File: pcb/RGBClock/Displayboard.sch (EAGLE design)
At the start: 66 parts, among them U1 LP3878MR-ADJ, U10 MCP23017SO, U2 P82B96DR, U3 P82B96DR, U4 PCA9685PW, U5 TPS71533DCKR, U6 ZXLD1362ET5TA, U7 74HCT1G14GW, U8 74HCT1G86GW, U9 TPA0172-HTSSOP24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

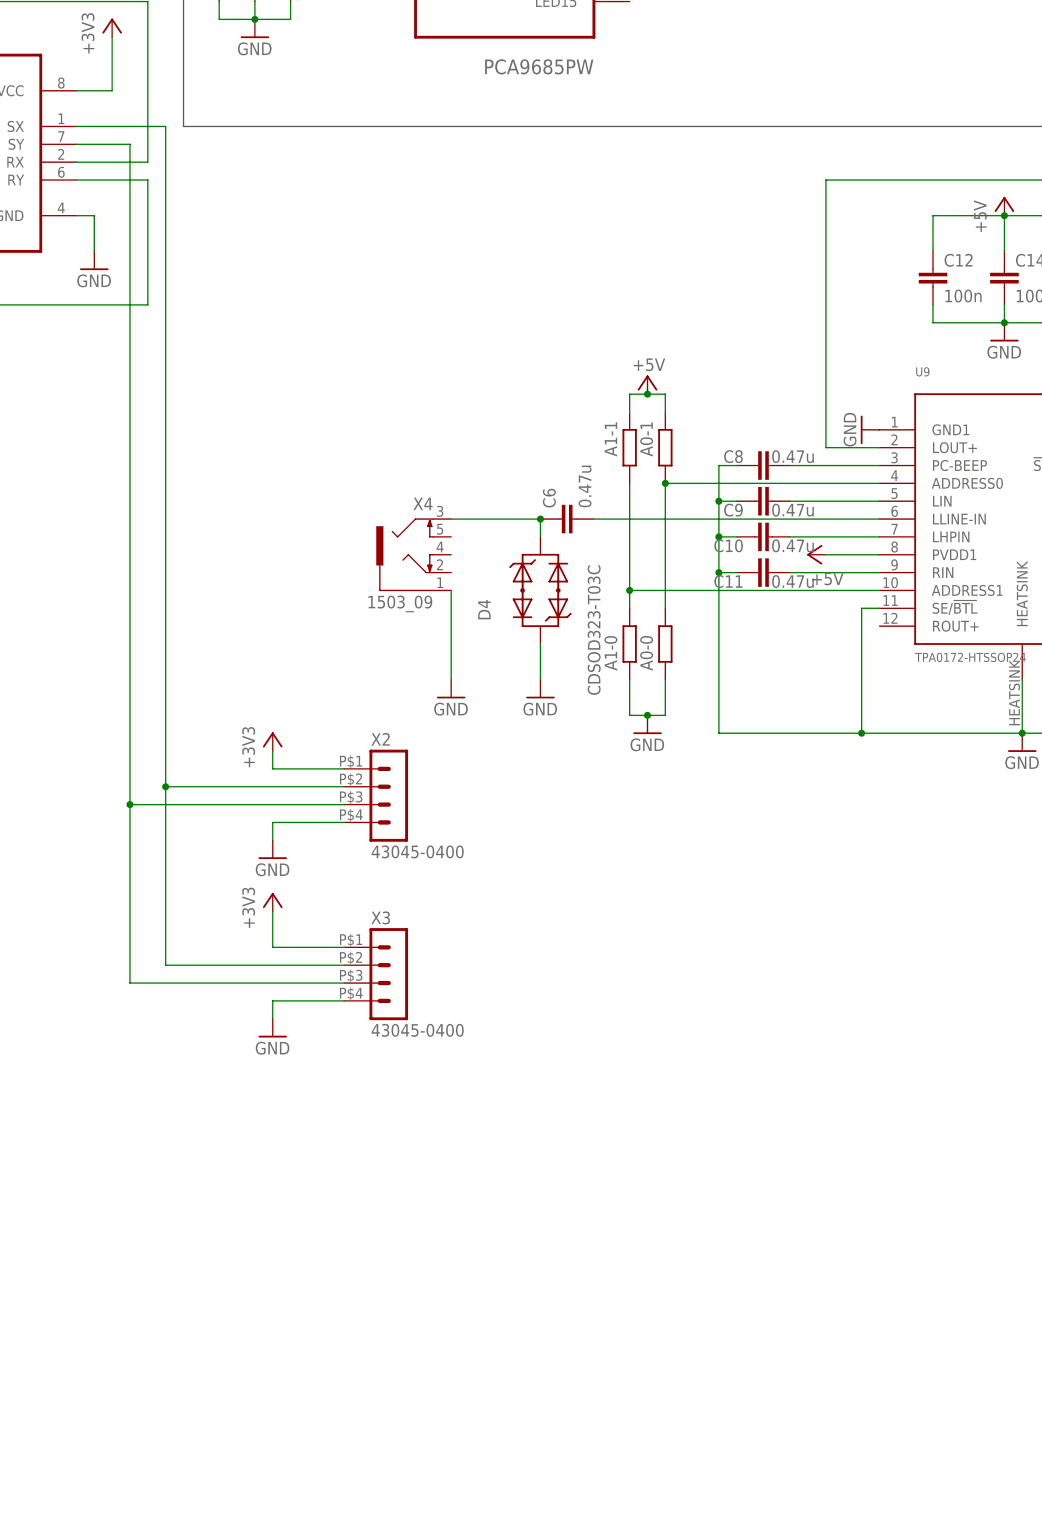
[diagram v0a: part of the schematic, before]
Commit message: Adding analog power and light sensor
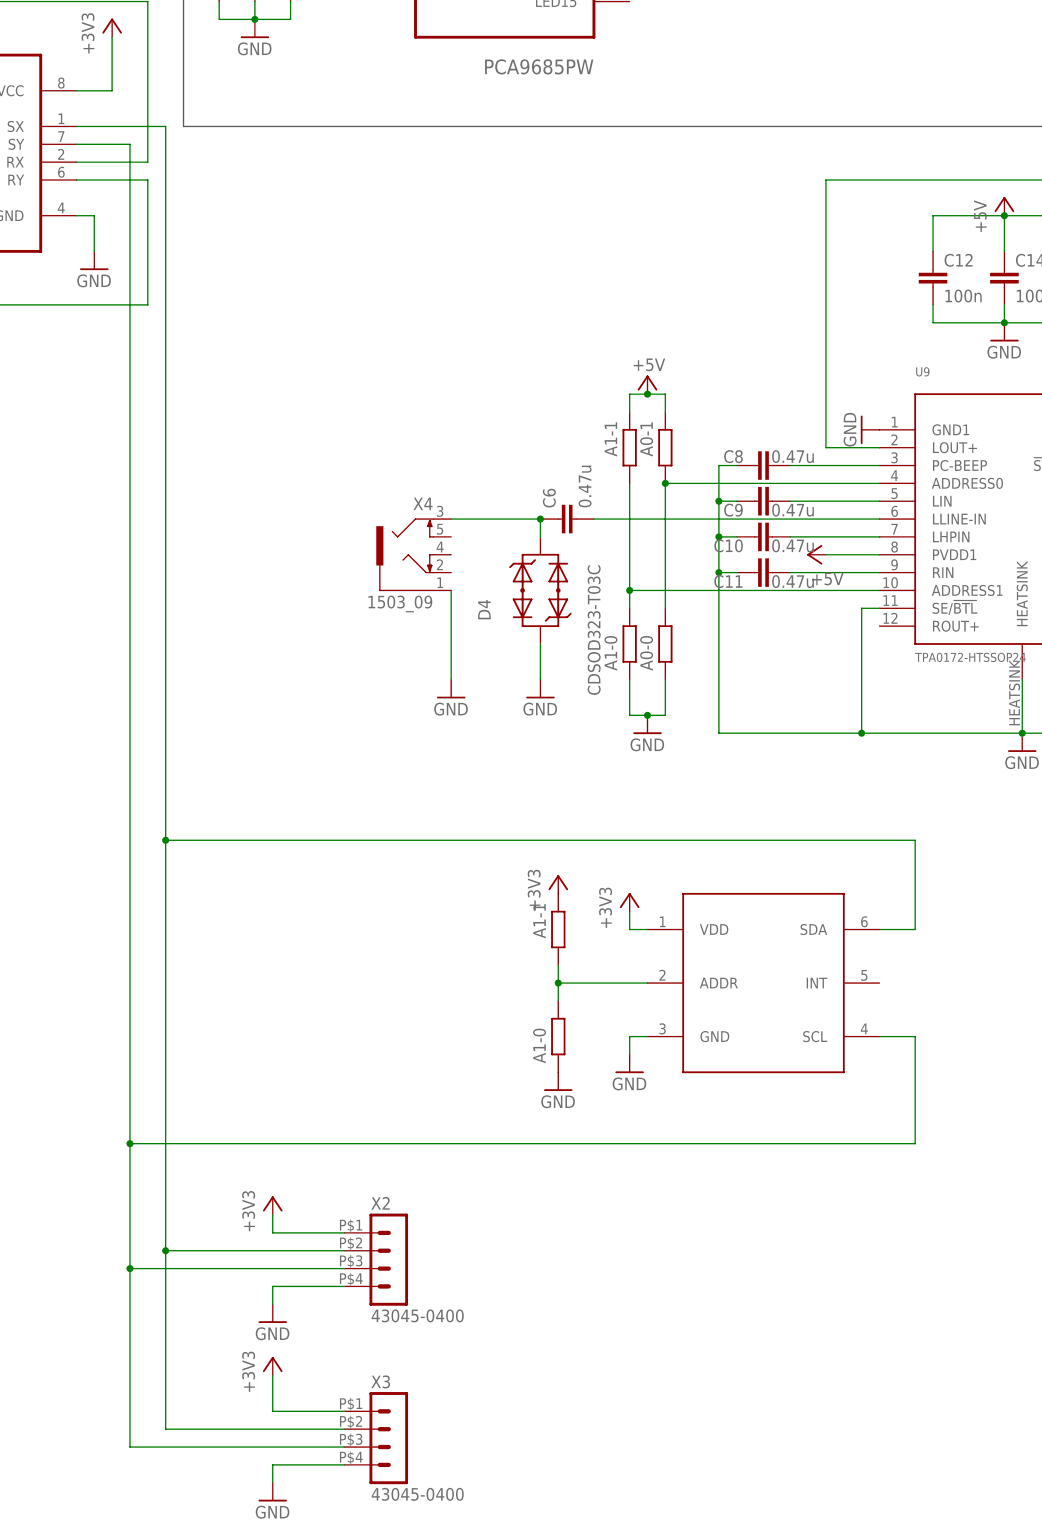
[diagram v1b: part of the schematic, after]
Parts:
- added R27: A1-1, resistor:R-EU_R0402
- added R28: A1-0, resistor:R-EU_R0402
- added U11: TSL2561, MyComponents:TSL2561
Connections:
- new net N$34: R27.1, R28.2, U11.ADDR
- net +3V3: now also R27.2, U11.VDD
- net GND: now also R28.1, U11.GND
- net N$7: now also U11.SDA
- net N$9: now also U11.SCL
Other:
- moved on the sheet: X2, X3
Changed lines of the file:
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@@
 <part name="C19" library="rcl" deviceset="C-EU" device="C0805" value="22n"/>
 <part name="GND27" library="supply1" deviceset="GND" device=""/>
+<part name="U11" library="MyComponents" deviceset="TSL2561" device=""/>
+<part name="GND28" library="supply1" deviceset="GND" device=""/>
+<part name="+3V5" library="supply1" deviceset="+3V3" device=""/>
+<part name="R27" library="resistor" deviceset="R-EU_" device="R0402" value="A1-1"/>
+<part name="R28" library="resistor" deviceset="R-EU_" device="R0402" value="A1-0"/>
+<part name="GND29" library="supply1" deviceset="GND" device=""/>
+<part name="+3V6" library="supply1" deviceset="+3V3" device=""/>
 </parts>
 <sheets>
@@
 <instance part="P+4" gate="1" x="383.54" y="-7.62" rot="R90"/>
 <instance part="GND5" gate="1" x="401.32" y="-12.7"/>
-<instance part="X2" gate="G$1" x="119.38" y="-96.52"/>
-<instance part="X3" gate="G$1" x="119.38" y="-121.92"/>
+<instance part="X2" gate="G$1" x="119.38" y="-162.56"/>
+<instance part="X3" gate="G$1" x="119.38" y="-187.96"/>
 <instance part="X5" gate="G$1" x="241.3" y="-10.16"/>
 <instance part="X6" gate="G$1" x="294.64" y="78.74"/>
-<instance part="+3V3" gate="G$1" x="104.14" y="-86.36"/>
-<instance part="+3V4" gate="G$1" x="104.14" y="-109.22"/>
-<instance part="GND7" gate="1" x="104.14" y="-104.14"/>
-<instance part="GND8" gate="1" x="104.14" y="-129.54"/>
+<instance part="+3V3" gate="G$1" x="104.14" y="-152.4"/>
+<instance part="+3V4" gate="G$1" x="104.14" y="-175.26"/>
+<instance part="GND7" gate="1" x="104.14" y="-170.18"/>
+<instance part="GND8" gate="1" x="104.14" y="-195.58"/>
 <instance part="GND9" gate="1" x="210.82" y="-88.9"/>
 <instance part="P+5" gate="1" x="248.92" y="-30.48"/>
@@
 </instance>
 <instance part="GND27" gate="1" x="342.9" y="-101.6"/>
+<instance part="U11" gate="G$1" x="172.72" y="-121.92"/>
+<instance part="GND28" gate="1" x="154.94" y="-134.62"/>
+<instance part="+3V5" gate="G$1" x="154.94" y="-109.22"/>
+<instance part="R27" gate="G$1" x="144.78" y="-114.3" smashed="yes" rot="R90">
+<attribute name="VALUE" x="143.002" y="-115.57" size="1.778" layer="96" rot="R90"/>
+</instance>
+<instance part="R28" gate="G$1" x="144.78" y="-129.54" smashed="yes" rot="R90">
+<attribute name="VALUE" x="143.002" y="-133.35" size="1.778" layer="96" rot="R90"/>
+</instance>
+<instance part="GND29" gate="1" x="144.78" y="-137.16"/>
+<instance part="+3V6" gate="G$1" x="144.78" y="-106.68"/>
 </instances>
 <busses>
@@
 <segment>
 <pinref part="GND7" gate="1" pin="GND"/>
-<wire x1="104.14" y1="-101.6" x2="104.14" y2="-99.06" width="0.1524" layer="91"/>
+<wire x1="104.14" y1="-167.64" x2="104.14" y2="-165.1" width="0.1524" layer="91"/>
 <pinref part="X2" gate="G$1" pin="4"/>
-<wire x1="104.14" y1="-99.06" x2="114.3" y2="-99.06" width="0.1524" layer="91"/>
+<wire x1="104.14" y1="-165.1" x2="114.3" y2="-165.1" width="0.1524" layer="91"/>
 </segment>
 <segment>
 <pinref part="GND8" gate="1" pin="GND"/>
-<wire x1="104.14" y1="-127" x2="104.14" y2="-124.46" width="0.1524" layer="91"/>
+<wire x1="104.14" y1="-193.04" x2="104.14" y2="-190.5" width="0.1524" layer="91"/>
 <pinref part="X3" gate="G$1" pin="4"/>
-<wire x1="104.14" y1="-124.46" x2="114.3" y2="-124.46" width="0.1524" layer="91"/>
+<wire x1="104.14" y1="-190.5" x2="114.3" y2="-190.5" width="0.1524" layer="91"/>
 </segment>
 <segment>
@@
 <pinref part="GND27" gate="1" pin="GND"/>
 </segment>
+<segment>
+<pinref part="R28" gate="G$1" pin="1"/>
+<pinref part="GND29" gate="1" pin="GND"/>
+</segment>
+<segment>
+<pinref part="U11" gate="G$1" pin="GND"/>
+<pinref part="GND28" gate="1" pin="GND"/>
+<wire x1="157.48" y1="-129.54" x2="154.94" y2="-129.54" width="0.1524" layer="91"/>
+<wire x1="154.94" y1="-129.54" x2="154.94" y2="-132.08" width="0.1524" layer="91"/>
+</segment>
 </net>
 <net name="VCC" class="2">
@@
 <segment>
 <pinref part="+3V3" gate="G$1" pin="+3V3"/>
-<wire x1="104.14" y1="-88.9" x2="104.14" y2="-91.44" width="0.1524" layer="91"/>
+<wire x1="104.14" y1="-154.94" x2="104.14" y2="-157.48" width="0.1524" layer="91"/>
 <pinref part="X2" gate="G$1" pin="1"/>
-<wire x1="104.14" y1="-91.44" x2="114.3" y2="-91.44" width="0.1524" layer="91"/>
+<wire x1="104.14" y1="-157.48" x2="114.3" y2="-157.48" width="0.1524" layer="91"/>
 </segment>
 <segment>
 <pinref part="+3V4" gate="G$1" pin="+3V3"/>
-<wire x1="104.14" y1="-111.76" x2="104.14" y2="-116.84" width="0.1524" layer="91"/>
+<wire x1="104.14" y1="-177.8" x2="104.14" y2="-182.88" width="0.1524" layer="91"/>
 <pinref part="X3" gate="G$1" pin="1"/>
-<wire x1="104.14" y1="-116.84" x2="114.3" y2="-116.84" width="0.1524" layer="91"/>
+<wire x1="104.14" y1="-182.88" x2="114.3" y2="-182.88" width="0.1524" layer="91"/>
+</segment>
+<segment>
+<pinref part="R27" gate="G$1" pin="2"/>
+<pinref part="+3V6" gate="G$1" pin="+3V3"/>
+</segment>
+<segment>
+<pinref part="+3V5" gate="G$1" pin="+3V3"/>
+<wire x1="154.94" y1="-111.76" x2="154.94" y2="-114.3" width="0.1524" layer="91"/>
+<pinref part="U11" gate="G$1" pin="VDD"/>
+<wire x1="154.94" y1="-114.3" x2="157.48" y2="-114.3" width="0.1524" layer="91"/>
 </segment>
 </net>
@@
 <pinref part="U3" gate="A" pin="SY"/>
 <wire x1="76.2" y1="-2.54" x2="83.82" y2="-2.54" width="0.1524" layer="91"/>
-<wire x1="83.82" y1="-2.54" x2="83.82" y2="-96.52" width="0.1524" layer="91"/>
+<wire x1="83.82" y1="-2.54" x2="83.82" y2="-144.78" width="0.1524" layer="91"/>
 <pinref part="X3" gate="G$1" pin="3"/>
-<wire x1="83.82" y1="-96.52" x2="83.82" y2="-121.92" width="0.1524" layer="91"/>
-<wire x1="83.82" y1="-121.92" x2="114.3" y2="-121.92" width="0.1524" layer="91"/>
+<wire x1="83.82" y1="-144.78" x2="83.82" y2="-162.56" width="0.1524" layer="91"/>
+<wire x1="83.82" y1="-162.56" x2="83.82" y2="-187.96" width="0.1524" layer="91"/>
+<wire x1="83.82" y1="-187.96" x2="114.3" y2="-187.96" width="0.1524" layer="91"/>
 <pinref part="X2" gate="G$1" pin="3"/>
-<wire x1="83.82" y1="-96.52" x2="114.3" y2="-96.52" width="0.1524" layer="91"/>
-<junction x="83.82" y="-96.52"/>
+<wire x1="83.82" y1="-162.56" x2="114.3" y2="-162.56" width="0.1524" layer="91"/>
+<junction x="83.82" y="-162.56"/>
+<pinref part="U11" gate="G$1" pin="SCL"/>
+<wire x1="190.5" y1="-129.54" x2="195.58" y2="-129.54" width="0.1524" layer="91"/>
+<wire x1="195.58" y1="-129.54" x2="195.58" y2="-144.78" width="0.1524" layer="91"/>
+<wire x1="195.58" y1="-144.78" x2="83.82" y2="-144.78" width="0.1524" layer="91"/>
+<junction x="83.82" y="-144.78"/>
 </segment>
 </net>
@@
 <pinref part="U3" gate="A" pin="SX"/>
 <wire x1="76.2" y1="0" x2="88.9" y2="0" width="0.1524" layer="91"/>
-<wire x1="88.9" y1="0" x2="88.9" y2="-93.98" width="0.1524" layer="91"/>
-<wire x1="88.9" y1="-93.98" x2="88.9" y2="-119.38" width="0.1524" layer="91"/>
+<wire x1="88.9" y1="0" x2="88.9" y2="-101.6" width="0.1524" layer="91"/>
+<wire x1="88.9" y1="-101.6" x2="88.9" y2="-160.02" width="0.1524" layer="91"/>
+<wire x1="88.9" y1="-160.02" x2="88.9" y2="-185.42" width="0.1524" layer="91"/>
 <pinref part="X2" gate="G$1" pin="2"/>
-<wire x1="88.9" y1="-93.98" x2="114.3" y2="-93.98" width="0.1524" layer="91"/>
-<junction x="88.9" y="-93.98"/>
+<wire x1="88.9" y1="-160.02" x2="114.3" y2="-160.02" width="0.1524" layer="91"/>
+<junction x="88.9" y="-160.02"/>
 <pinref part="X3" gate="G$1" pin="2"/>
-<wire x1="88.9" y1="-119.38" x2="114.3" y2="-119.38" width="0.1524" layer="91"/>
+<wire x1="88.9" y1="-185.42" x2="114.3" y2="-185.42" width="0.1524" layer="91"/>
+<wire x1="88.9" y1="-101.6" x2="195.58" y2="-101.6" width="0.1524" layer="91"/>
+<wire x1="195.58" y1="-101.6" x2="195.58" y2="-114.3" width="0.1524" layer="91"/>
+<pinref part="U11" gate="G$1" pin="SDA"/>
+<wire x1="195.58" y1="-114.3" x2="190.5" y2="-114.3" width="0.1524" layer="91"/>
+<junction x="88.9" y="-101.6"/>
 </segment>
 </net>
@@
 </segment>
 </net>
+<net name="N$34" class="0">
+<segment>
+<pinref part="R27" gate="G$1" pin="1"/>
+<pinref part="R28" gate="G$1" pin="2"/>
+<wire x1="144.78" y1="-119.38" x2="144.78" y2="-121.92" width="0.1524" layer="91"/>
+<wire x1="144.78" y1="-121.92" x2="144.78" y2="-124.46" width="0.1524" layer="91"/>
+<pinref part="U11" gate="G$1" pin="ADDR"/>
+<wire x1="144.78" y1="-121.92" x2="157.48" y2="-121.92" width="0.1524" layer="91"/>
+<junction x="144.78" y="-121.92"/>
+</segment>
+</net>

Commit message: Main and Display updated
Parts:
- C1, C7: device rcl:C-EUC1206 -> rcl:C-EUC0805
- C15, C4: device rcl:C-EUC2012 -> rcl:C-EUC0805
- C2, C3: device rcl:C-EUC1608 -> rcl:C-EUC0805
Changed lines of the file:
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@@
 <setting verticaltext="up"/>
 </settings>
-<grid distance="0.1" unitdist="inch" unit="inch" style="lines" multiple="1" display="no" altdistance="0.01" altunitdist="inch" altunit="inch"/>
+<grid distance="50" unitdist="mil" unit="mil" style="lines" multiple="1" display="no" altdistance="0.01" altunitdist="inch" altunit="inch"/>
 <layers>
 <layer number="1" name="Top" color="4" fill="1" visible="no" active="no"/>
@@
 <part name="P+8" library="supply1" deviceset="+5V" device=""/>
 <part name="C5" library="rcl" deviceset="C-EU" device="C0805" value="100n"/>
-<part name="C7" library="rcl" deviceset="C-EU" device="C1206" value="0,47u"/>
+<part name="C7" library="rcl" deviceset="C-EU" device="C0805" value="0,47u"/>
 <part name="C12" library="rcl" deviceset="C-EU" device="C0805" value="100n"/>
 <part name="C14" library="rcl" deviceset="C-EU" device="C0805" value="100n"/>
@@
 <part name="GND19" library="supply1" deviceset="GND" device=""/>
 <part name="C18" library="rcl" deviceset="C-EU" device="C0805" value="0.47u"/>
-<part name="C15" library="rcl" deviceset="C-EU" device="C2012" value="10u"/>
-<part name="C1" library="rcl" deviceset="C-EU" device="C1206" value="4u7"/>
-<part name="C2" library="rcl" deviceset="C-EU" device="C1608" value="10n"/>
-<part name="C3" library="rcl" deviceset="C-EU" device="C1608" value="680p"/>
+<part name="C15" library="rcl" deviceset="C-EU" device="C0805" value="10u"/>
+<part name="C1" library="rcl" deviceset="C-EU" device="C0805" value="4u7"/>
+<part name="C2" library="rcl" deviceset="C-EU" device="C0805" value="10n"/>
+<part name="C3" library="rcl" deviceset="C-EU" device="C0805" value="680p"/>
 <part name="R1" library="resistor" deviceset="R-EU_" device="R0603" value="4.02k"/>
 <part name="R2" library="resistor" deviceset="R-EU_" device="R0603" value="1k"/>
 <part name="GND20" library="supply1" deviceset="GND" device=""/>
-<part name="C4" library="rcl" deviceset="C-EU" device="C2012" value="10u"/>
+<part name="C4" library="rcl" deviceset="C-EU" device="C0805" value="10u"/>
 <part name="GND21" library="supply1" deviceset="GND" device=""/>
 <part name="GND22" library="supply1" deviceset="GND" device=""/>
@@
 <instance part="GND19" gate="1" x="172.72" y="114.3"/>
 <instance part="C18" gate="G$1" x="256.54" y="-76.2" smashed="yes" rot="R180">
-<attribute name="NAME" x="262.636" y="-76.581" size="1.778" layer="95" rot="R180"/>
-<attribute name="VALUE" x="265.176" y="-71.501" size="1.778" layer="96" rot="R180"/>
+<attribute name="NAME" x="262.636" y="-71.501" size="1.778" layer="95" rot="R180"/>
+<attribute name="VALUE" x="263.906" y="-76.581" size="1.778" layer="96" rot="R180"/>
 </instance>
 <instance part="C15" gate="G$1" x="218.44" y="-20.32"/>
